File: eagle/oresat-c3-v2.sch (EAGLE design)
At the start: 168 parts, among them J1 J-SAMTEC-TFM-110-X1-XXX-D-RA, J10 U.FL, J11 U.FL, J13 U.FL, J14 U.FL, J15 HARWIN-2X8X1.27, J19 HARWIN-2X8X1.27, J2 U.FL, J3 U.FL, J4 U.FL, J6 J-SAMTEC-TFM-120-X1-XXX-D-RA, J7 FTSH-105-XX-X-DV-K, J8 U.FL, J9 U.FL, Q1 MOSFET-PCH-SOT23-6, U1 MAX892LEUA+T21-0036K-L, U11 U-ONSEMI-AX5043, U12 LP2985XX-N, U13 U-ONSEMI-AX5043, U14 LP2985XX-N, U2 TCAN330, U3 TCAN330, U4 TPS259621 - eFuse, U5 TPS62111RSA, U6 MAX6374KA-T21-0078H-L, U7 STM32F446RE, U9 SFEM016GB1EM1TO-A-HG-111-STD, X1 16MHZ-2.5x2mm, X3 TAITIEN-TY, X4 TAITIEN-TY

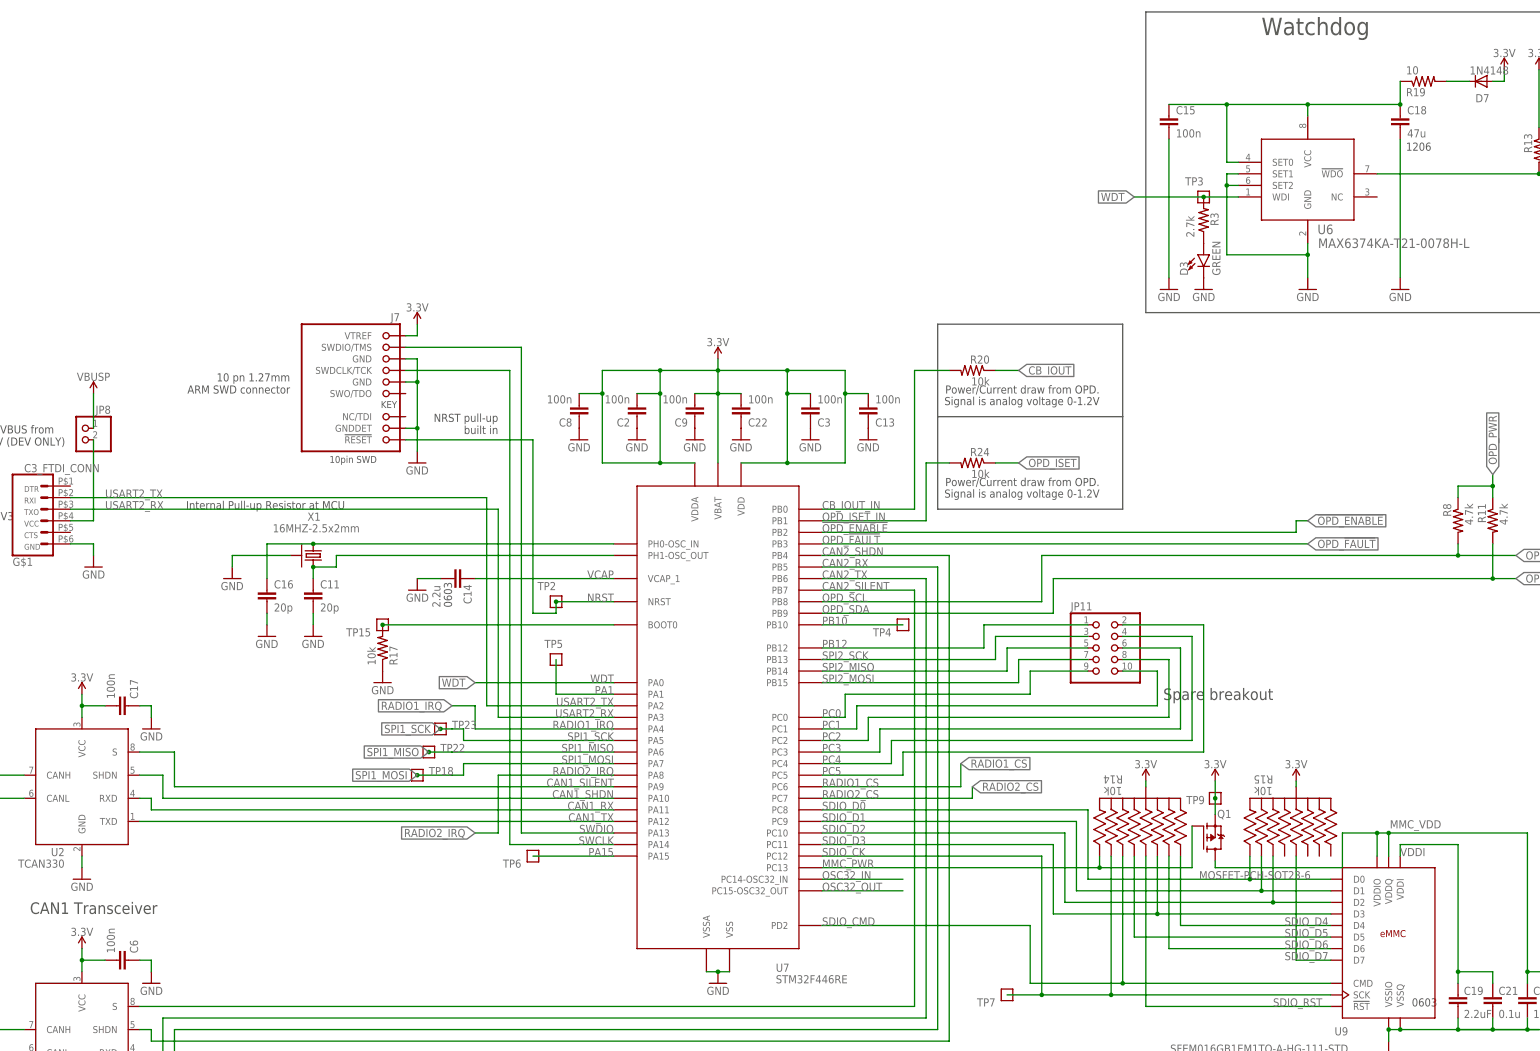
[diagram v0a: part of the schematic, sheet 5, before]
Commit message: Replacing non 0603 with 0603 package equivalents
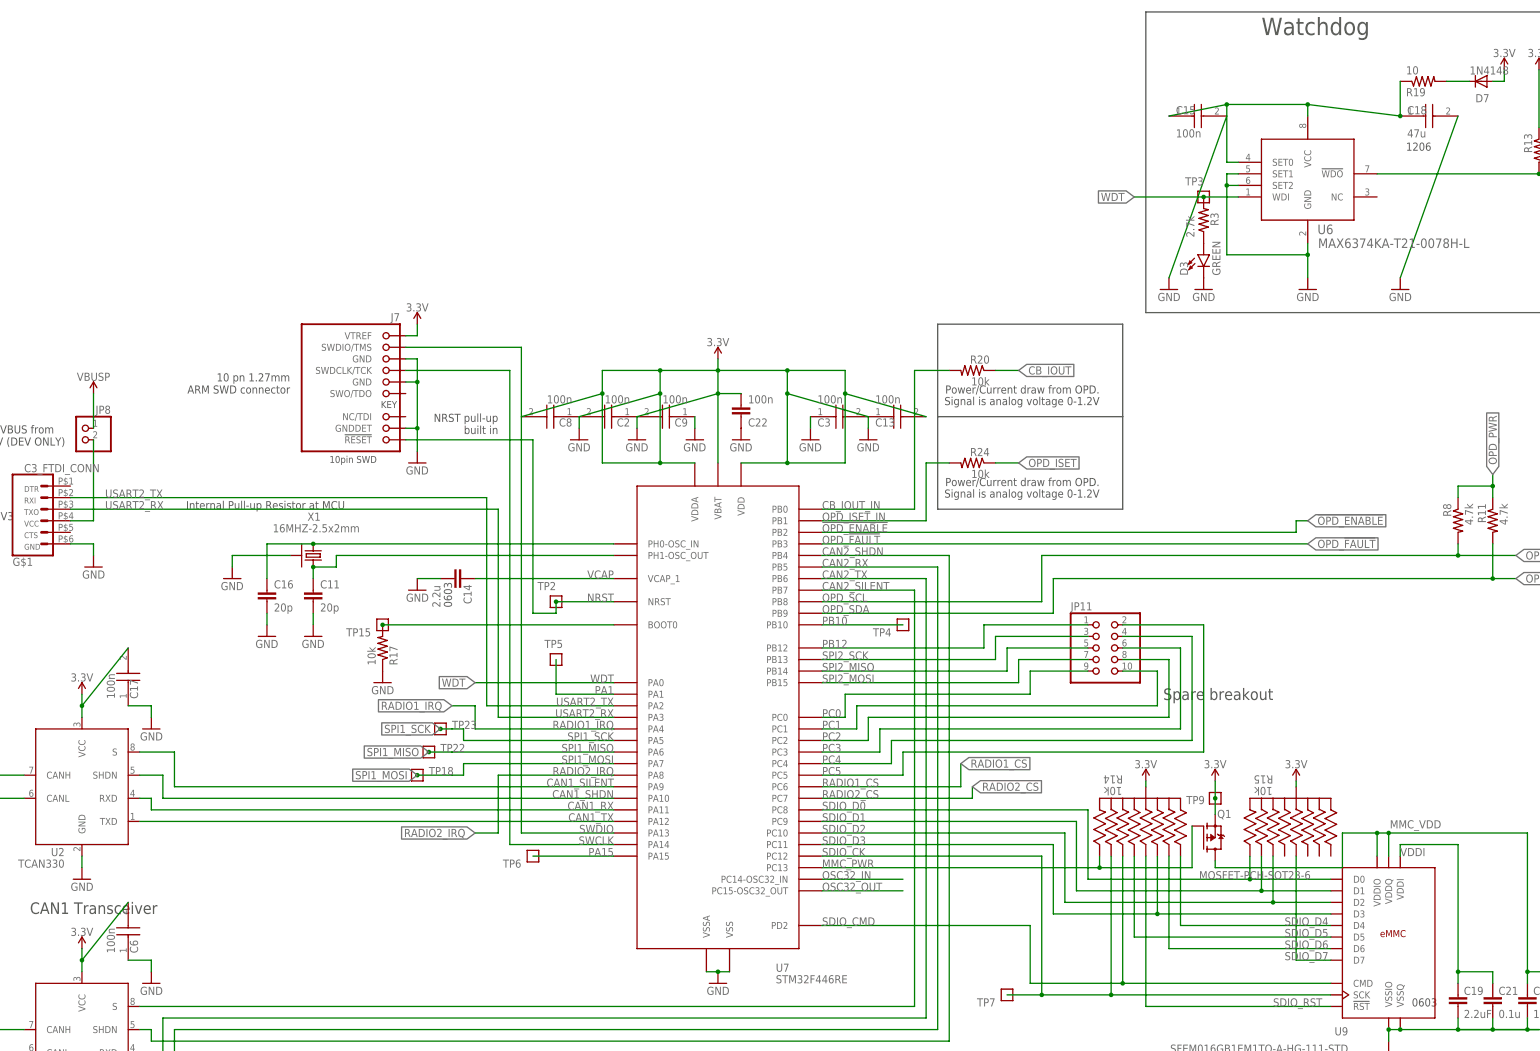
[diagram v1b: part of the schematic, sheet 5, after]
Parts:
- C13, C15, C17, C2, C3, C6, C8, C9: device oresat-rcl:C-EU0402-B-NOSILK -> SamacSys_Parts:C0603X104K5RAC3316
- C18: device oresat-rcl:C-EU1206-B -> SamacSys_Parts:GRM188R60J476ME15D

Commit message: Replaced non 0603 passive components with available 0603 equivalents
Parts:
- C1, C23, C24, C25, C4, C5: value 1u -> 1uF; device oresat-rcl:C-EU0603-B-NOSILK -> C3_SamacSys_Parts:CAP0603-1UF
- C10: value 1u -> 10uF; device oresat-rcl:C-EU0603-B-NOSILK -> C3_SamacSys_Parts:CAP0603-10UF
- C11: value 20p -> 20pF; device rcl_custom:C-EU0402-B-NOSILK -> C3_SamacSys_Parts:CAP0603-20PF
- C12: value 22u -> 22pF; device oresat-rcl:C-EU0805-B-NOSILK -> C3_SamacSys_Parts:CAP0603-22PF
- C13, C15, C17, C2, C3, C6, C8, C9: value 100n -> 0.1uf; device SamacSys_Parts:C0603X104K5RAC3316 -> C3_SamacSys_Parts:CAP0603-0.1UF
- C14: value 2.2u -> 2.2uF; device oresat-rcl:C-EU0603-B-NOSILK -> C3_SamacSys_Parts:CAP0603-2.2UF
- C16: value 20p -> 20pF; device oresat-rcl:C-EU0402-B-NOSILK -> C3_SamacSys_Parts:CAP0603-20PF
- C18: value 47u -> 47uF; device SamacSys_Parts:GRM188R60J476ME15D -> C3_SamacSys_Parts:CAP0603-47UF
- C19: device oresat-rcl:C-EU0603-B-NOSILK -> C3_SamacSys_Parts:CAP0603-2.2UF
- C21: value 0.1u -> 0.1uf; device oresat-rcl:C-EU0603-B-NOSILK -> C3_SamacSys_Parts:CAP0603-0.1UF
- C22: value 100n -> 0.1uf; device oresat-rcl:C-EU0402-B-NOSILK -> C3_SamacSys_Parts:CAP0603-0.1UF
- C26: device oresat-rcl:C-EU0603-B-NOSILK -> C3_SamacSys_Parts:CAP0603-10UF
- C42, C43, C58, C59: value 8.2p -> 8.2pF; device oresat-rcl:C-EU0402-C-NOSILK -> C3_SamacSys_Parts:CAP0603-8.2PF
- C44, C45, C60, C61: value 1n -> 1000pF; device oresat-rcl:C-EU0402-C-NOSILK -> C3_SamacSys_Parts:CAP0603-1000PF
- C46, C47, C62, C63: value 82p -> 82pF; device oresat-rcl:C-EU0402-C-NOSILK -> C3_SamacSys_Parts:CAP0603-82PF
- C48, C49, C64, C65: value 22p -> 22pF; device oresat-rcl:C-EU0402-C-NOSILK -> C3_SamacSys_Parts:CAP0603-22PF
- C50, C53, C66, C69: value 22n -> 0.022uF; device oresat-rcl:C-EU0603-C-NOSILK -> C3_SamacSys_Parts:CAP0603-0.022UF
- C51, C54: value NP -> 0.022uF; device oresat-rcl:C-EU0603-C-NOSILK -> C3_SamacSys_Parts:CAP0603-0.022UF
- C52, C55, C68, C71: value 4.7u -> 4.7uF; device oresat-rcl:C-EU0603-C-NOSILK -> C3_SamacSys_Parts:CAP0603-4.7UF
- C56, C72: device oresat-rcl:C-EU0603-C-NOSILK -> C3_SamacSys_Parts:CAP0603-0.01UF
- C57, C73: value 1u -> 1uF; device oresat-rcl:C-EU0603-C-NOSILK -> C3_SamacSys_Parts:CAP0603-1UF
- C67, C70: value NP -> 0.1uf; device oresat-rcl:C-EU0603-C-NOSILK -> C3_SamacSys_Parts:CAP0603-0.1UF
- C7: value 10u -> 10uF; device oresat-rcl:C-EU0805-B-NOSILK -> C3_SamacSys_Parts:CAP0603-10UF
- R1, R2, R3, R4: device oresat-rcl:R-US_0402-B-NOSILK -> C3_SamacSys_Parts:R0603-2.7K-OHMS
- R10: device oresat-rcl:R-US_0402-B-NOSILK -> C3_SamacSys_Parts:R0603-0-OHMS
- R11, R13, R8: device oresat-rcl:R-US_0402-B-NOSILK -> C3_SamacSys_Parts:R0603-4.7K-OHMS
- R12: device oresat-rcl:R-US_0603-B-NOSILK -> C3_SamacSys_Parts:R0603-0-OHMS
- R16, R17, R20, R24, R27, R7, R9: device oresat-rcl:R-US_0402-B-NOSILK -> C3_SamacSys_Parts:R0603-10K-OHMS
- R19: device oresat-rcl:R-US_0402-B-NOSILK -> C3_SamacSys_Parts:R0603-10-OHMS
- R28, R34: device oresat-rcl:R-US_0402-C-NOSILK -> C3_SamacSys_Parts:R0603-150-OHMS
- R32, R33, R39, R40: device oresat-rcl:R-US_0603-C-NOSILK -> C3_SamacSys_Parts:R0603-0-OHMS
- R36: value 23.9k -> 23.7k; device oresat-rcl:R-US_0402-B-NOSILK -> C3_SamacSys_Parts:R0603-23.7K-OHMS
- R5: value 31.7k -> 31.6k; device oresat-rcl:R-US_0402-B-NOSILK -> C3_SamacSys_Parts:R0603-31.6K-OHMS
- R6: device oresat-rcl:R-US_0402-B-NOSILK -> C3_SamacSys_Parts:R0603-3.1K-OHMS

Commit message: Parts Move so far
not completed
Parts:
- removed JP11, JP2: (no value), pinhead:PINHD-2X5
- removed JP4, JP6: (no value), J-2X8X1.27:PINHD-1X2
- removed TP9: TEST-POINT, Tova:TEST-POINT
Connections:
- net !SD renamed SD
- removed net SPARE1: J6.10, J6.9, JP2.5
- removed net SPARE2: J6.7, J6.8, JP2.4
- removed net SPARE3: J6.5, J6.6, JP2.3
- removed net SPARE4: J6.3, J6.4, JP2.2
- removed net SPARE5: J6.1, J6.2, JP2.1
- net 3.3V: no longer JP6.1, JP6.2, TP9.1
- net GND: no longer JP2.10, JP2.7, JP2.8, JP2.9
- net MMC_PWR: now also R15.66; no longer R14.11
- net PB12: no longer JP11.1
- net PC0: no longer JP11.9
- net PC1: no longer JP11.10
- net PC2: no longer JP11.8
- net PC3: no longer JP11.6
- net PC4: no longer JP11.4
- net PC5: no longer JP11.2
- net SDIO_CK: now also R14.22; no longer R14.99
- net SDIO_CMD: now also R14.99; no longer R14.22
- net SPI2_MISO: no longer JP11.5
- net SPI2_MOSI: no longer JP11.7
- net SPI2_SCK: no longer JP11.3
- net VBUSP: no longer JP4.1, JP4.2
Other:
- note removed: "Spare breakout"
- moved on the sheet: Q1

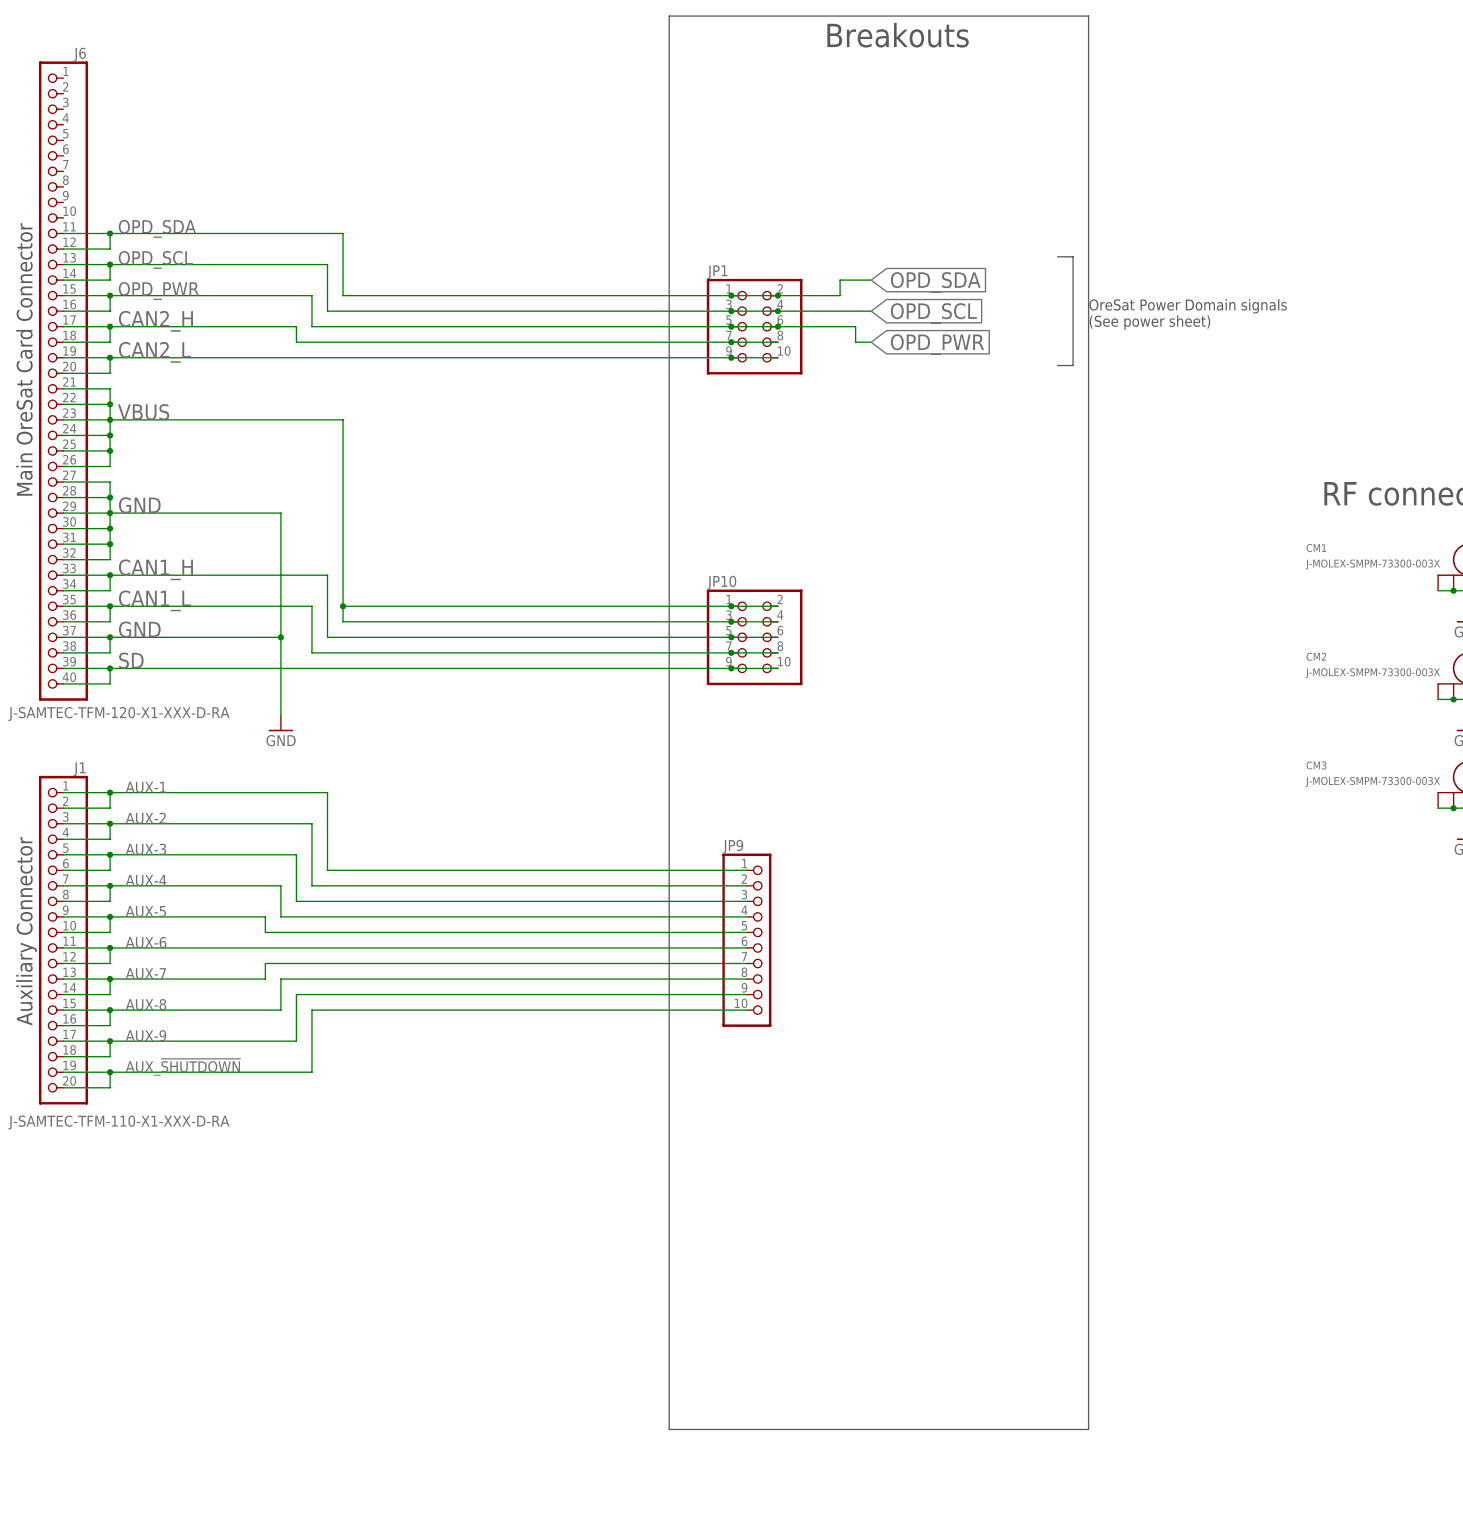
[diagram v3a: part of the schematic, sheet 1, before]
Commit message: Removed Jumpers and moved eMMC, processor, and more
Mostly reconnected , made changed to some of the polygons
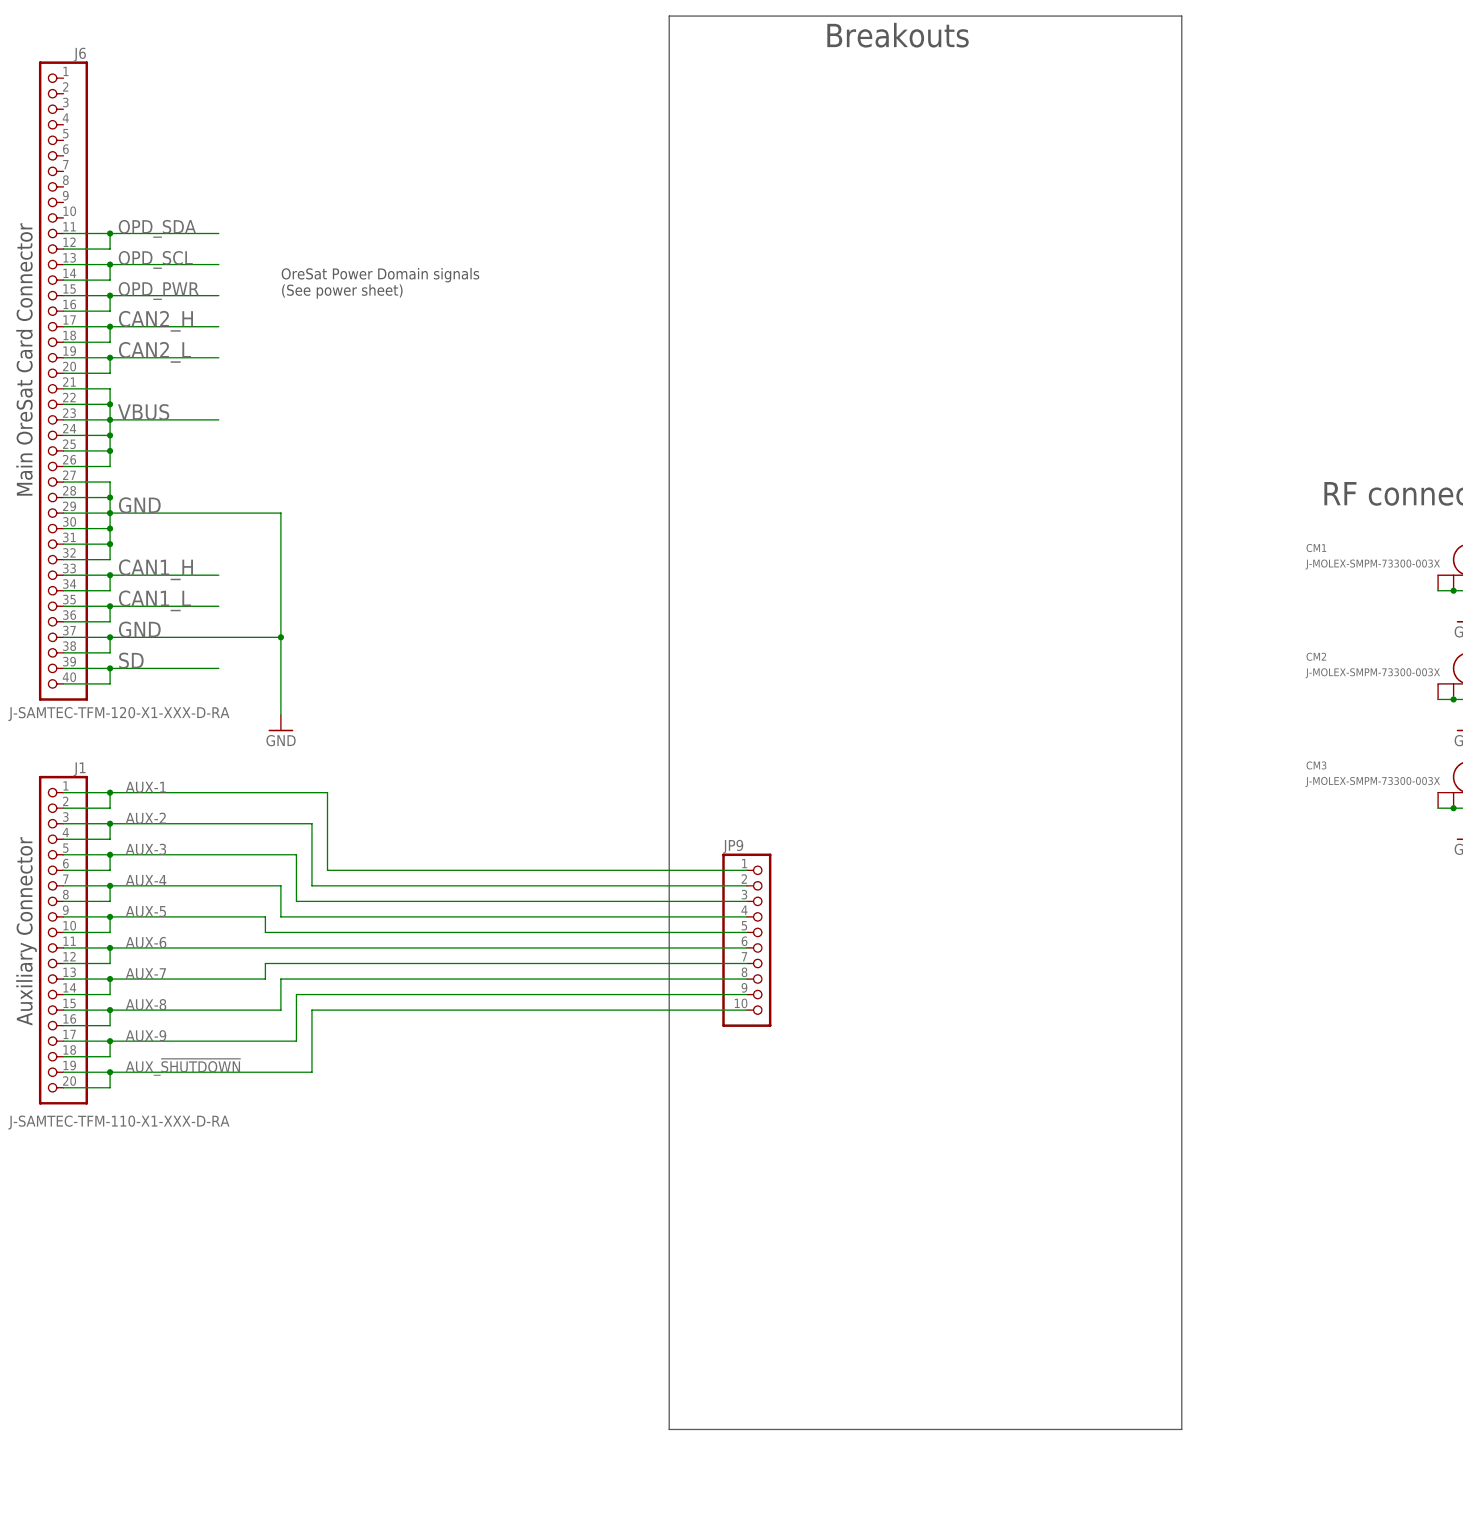
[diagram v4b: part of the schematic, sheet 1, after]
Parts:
- removed JP1, JP10: (no value), pinhead:PINHD-2X5
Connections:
- net CAN1_H: no longer JP10.5, JP10.6
- net CAN1_L: no longer JP10.7, JP10.8
- net CAN2_H: no longer JP1.7, JP1.8
- net CAN2_L: no longer JP1.10, JP1.9
- net OPD_PWR: no longer JP1.5, JP1.6
- net OPD_SCL: no longer JP1.3, JP1.4
- net OPD_SDA: no longer JP1.1, JP1.2
- net SD: no longer JP10.10, JP10.9
- net VBUS: no longer JP10.1, JP10.2, JP10.3, JP10.4
